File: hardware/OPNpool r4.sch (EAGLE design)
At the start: 16 parts, among them J2 RS485-TERM-SPTAF, J3 ESP-JTAG-2X05, SW1 Factory (5 sec), U1 MAX3485CSA+

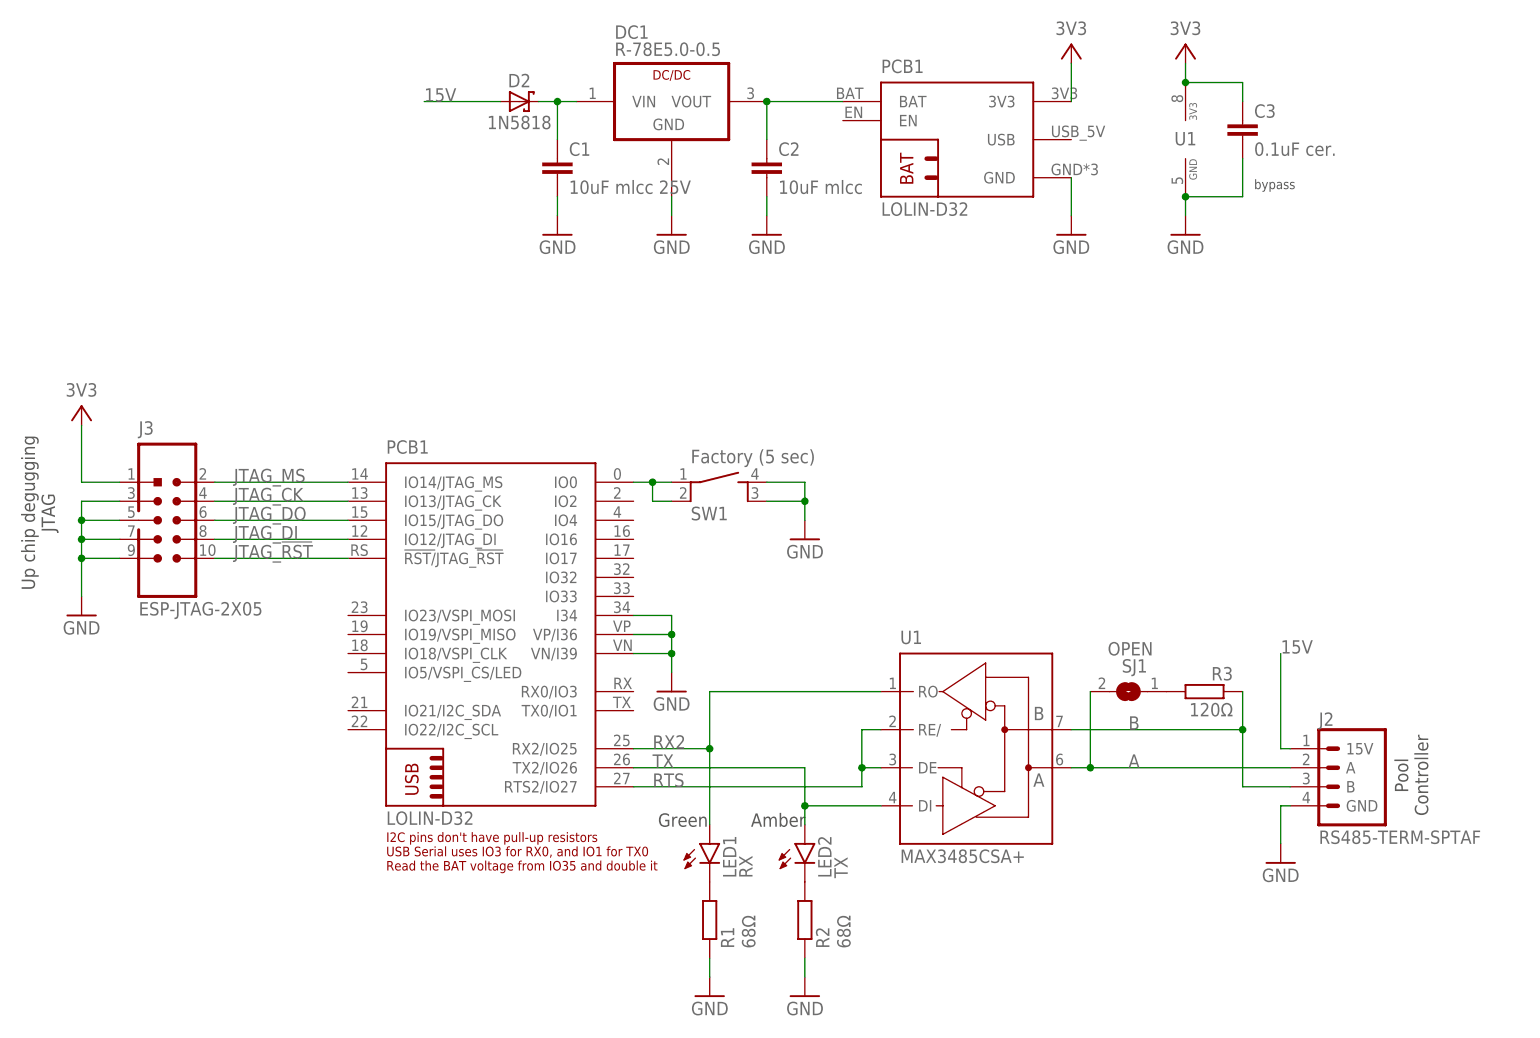
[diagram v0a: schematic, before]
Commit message: switch to esp32-c6-devkitc-1 module
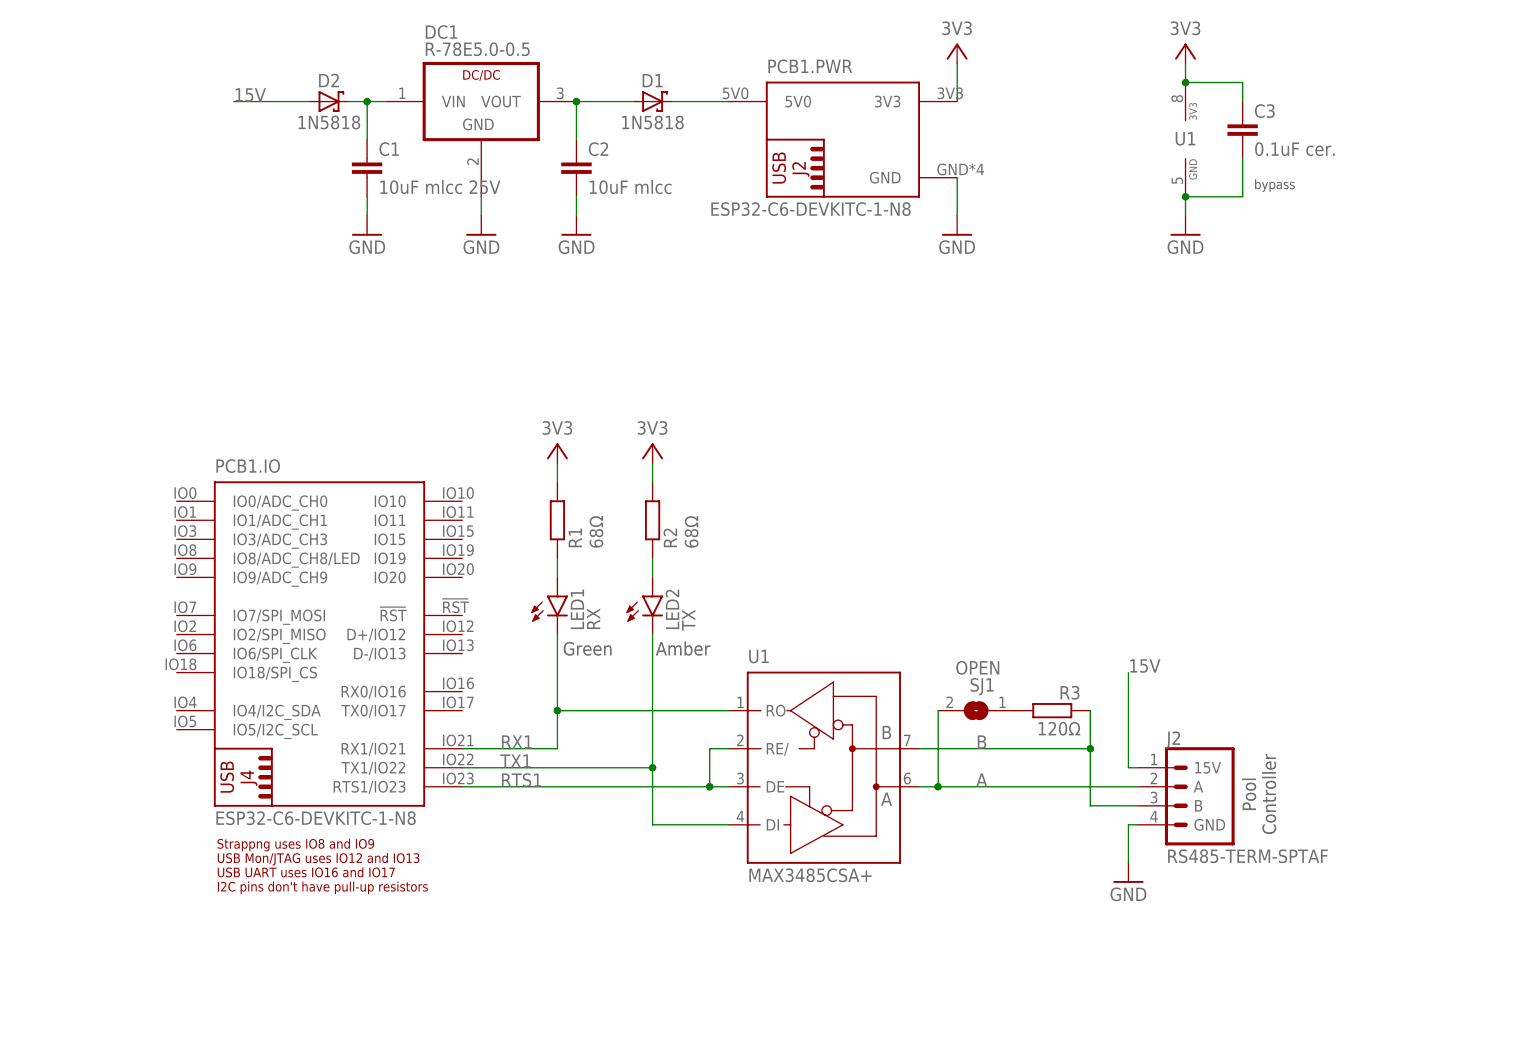
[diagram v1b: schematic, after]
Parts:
- removed J3: ESP-JTAG-2X05, Coert Vonk:ESP-JTAG-2X05
- removed SW1: Factory (5 sec), 1-1825910-4:1-1825910-4
- added D1: 1N5818, Coert Vonk:1N5818
- PCB1: value LOLIN-D32 -> ESP32-C6-DEVKITC-1-N8; device Coert Vonk:LOLIN-D32 -> Coert-Vonk:ESP32-C6-DEVKITC-1-N8; ALIEXPRESS# 32808551116 -> (none); MANF WEMOS Electronics -> (none); MANF# D32 -> (none)
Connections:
- removed net JTAG_!RST: J3.NC, PCB1G$1.!RST/!JTAG_!RST
- removed net JTAG_CK: J3.TCK, PCB1G$1.IO13/JTAG_CK
- removed net JTAG_DI: J3.TDI, PCB1G$1.IO12/JTAG_DI
- removed net JTAG_DO: J3.TDO, PCB1G$1.IO15/JTAG_DO
- removed net JTAG_MS: J3.TMS, PCB1G$1.IO14/JTAG_MS
- removed net N$3: PCB1G$1.IO0, SW1.1, SW1.2
- removed net RTS: PCB1G$1.RTS2/IO27, U1G$1.DE, U1G$1.RE/
- removed net RX2: LED1.A, PCB1G$1.RX2/IO25, U1G$1.RO
- removed net TX: LED2.A, PCB1G$1.TX2/IO26, U1G$1.DI
- new net N$4: D1.C, PCB1.PWR.5V0
- new net RTS1: PCB1.IO.RTS1/IO23, U1G$1.DE, U1G$1.RE/
- new net RX1: LED1.C, PCB1.IO.RX1/IO21, U1G$1.RO
- new net TX1: LED2.C, PCB1.IO.TX1/IO22, U1G$1.DI
- net 3V3: now also PCB1.PWR.3V3, R1.2, R2.2; no longer J3.3V3, PCB1P.3V3
- net GND: now also PCB1.PWR.GND; no longer J3.GND, J3.GND@1, J3.GND@2, J3.GND@3, PCB1G$1.I34, PCB1G$1.VN/I39, PCB1G$1.VP/I36, PCB1P.GND, R1.1, R2.1, SW1.3, SW1.4
- net N$1: now also LED1.A, R1.1; no longer LED1.C, R1.2
- net N$2: now also LED2.A, R2.1; no longer LED2.C, R2.2
- net VOUT: now also D1.A; no longer PCB1P.BAT
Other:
- note removed: "Up chip degugging JTAG"
- moved on the sheet: C1, C2, D2, DC1, J2, LED1, LED2, R1, R2, R3, SJ1, U1
